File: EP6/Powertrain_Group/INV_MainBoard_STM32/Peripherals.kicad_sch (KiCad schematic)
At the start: 26 parts, among them U4 TCAN1042VDRQ1, U5 CAT24C256, U6 TCAN1042VDRQ1

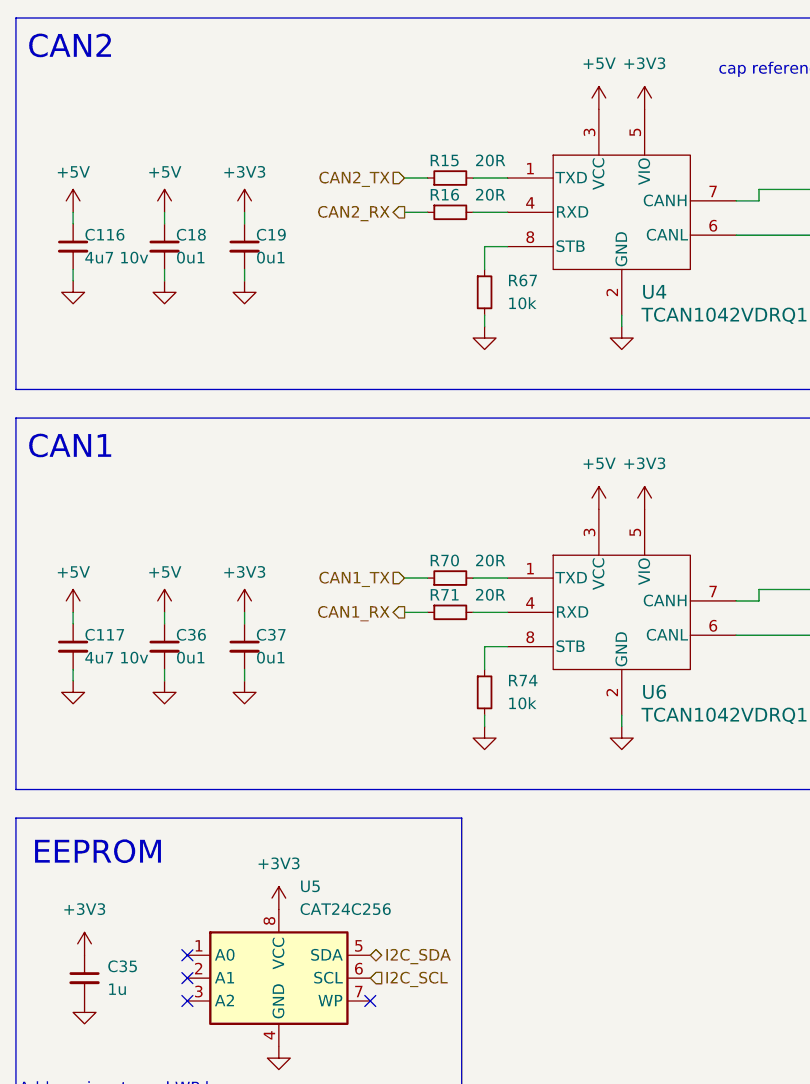
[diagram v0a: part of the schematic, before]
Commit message: update INV_MainBoard_STM32 to V2.1
update for JLCPCB, include change in 1.65 Vref and some name change for easier JLCPCBA BOM selection
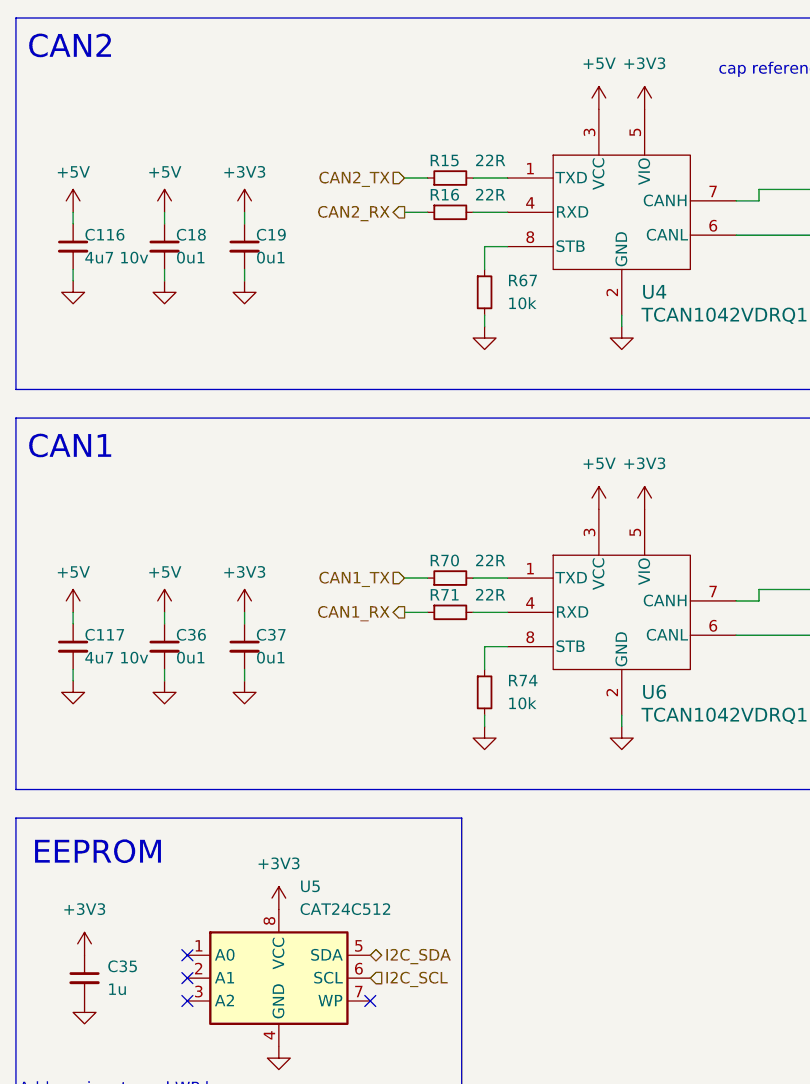
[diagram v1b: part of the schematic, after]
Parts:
- R15, R16, R70, R71: value 20R -> 22R
- U5: value CAT24C256 -> CAT24C512
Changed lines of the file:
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@@
 	(title_block
 		(title "INV_MainBoard_STM32")
-		(rev "2.0")
+		(date "2025-02-28")
+		(rev "2.1")
 		(company "NTURacing Team")
 		(comment 1 "郭哲明 Jack Kuo")
@@
 			)
 		)
-		(property "Value" "20R"
+		(property "Value" "22R"
 			(at 66.675 34.925 90)
 			(effects
@@
 			)
 		)
-		(property "Value" "CAT24C256"
+		(property "Value" "CAT24C512"
 			(at 45.4935 114.3 0)
 			(effects
@@
 			)
 		)
-		(property "Value" "20R"
+		(property "Value" "22R"
 			(at 66.675 31.115 90)
 			(effects
@@
 			)
 		)
-		(property "Value" "20R"
+		(property "Value" "22R"
 			(at 66.675 79.375 90)
 			(effects
@@
 			)
 		)
-		(property "Value" "20R"
+		(property "Value" "22R"
 			(at 66.675 75.565 90)
 			(effects

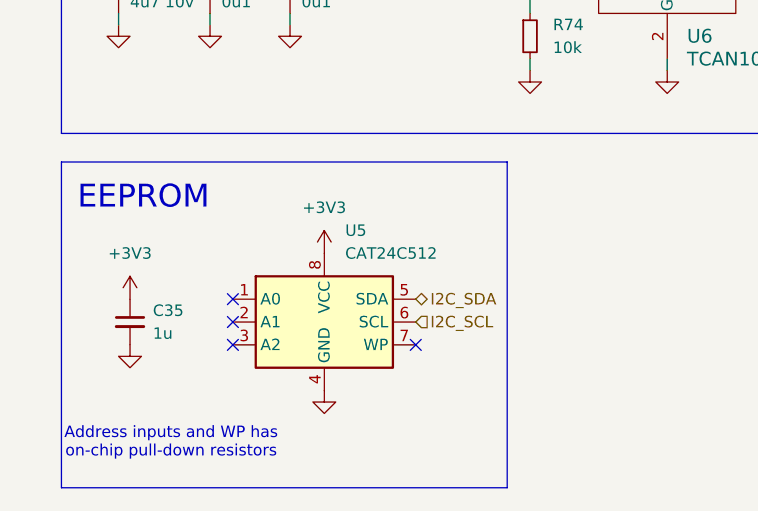
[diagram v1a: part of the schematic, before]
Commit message: update INV_MainBoard_STM32 to V3.0
PCB: INV_MainBoard_STM32 V3.0
V3.0 remove low volte trig
     add RC filt for OCP, OTP
     dedicated OTP, OCP pull down gate enable
     pending: fault hardware OTP/OCP latch
     pending: add QSPI DRAM
     use JST PH
     exterinal pull up for flt, ready
     fix CAN1, 2 label on board
     use 1k, 2k for encoder divider
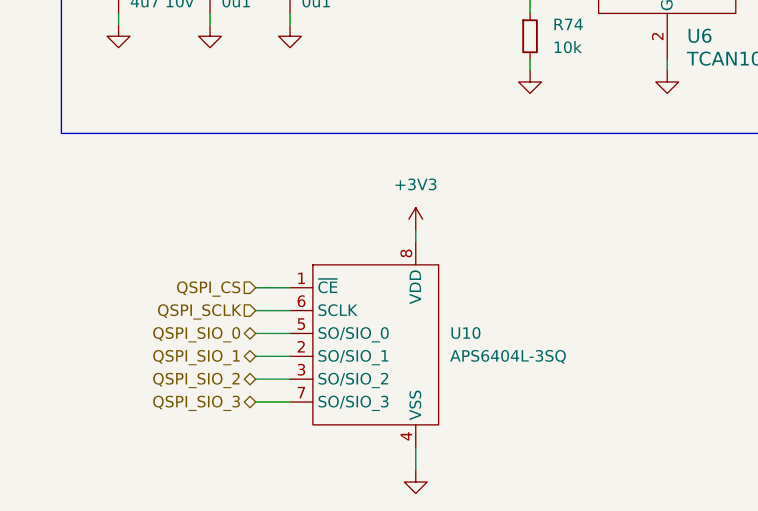
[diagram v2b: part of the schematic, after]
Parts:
- removed C35: 1u, Capacitor_SMD:C_0402_1005Metric, symbol Device:C_Small
- removed U5: CAT24C512, Package_SO:SOIC-8_3.9x4.9mm_P1.27mm, symbol Memory_EEPROM:CAT24C256
- added U10: APS6404L-3SQ, Package_SO:SOP-8_3.76x4.96mm_P1.27mm, symbol nturt_kicad_lib_EP6:APS6404L-3SQ
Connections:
- net +3V3: now also U10.8 (VDD)
- net GND: now also U10.4 (VSS)
- new net QSPI_CS: U10.1 (~{CE})
- new net QSPI_SCLK: U10.6 (SCLK)
- new net QSPI_SIO_0: U10.5 (SO/SIO_0)
- new net QSPI_SIO_1: U10.2 (SO/SIO_1)
- new net QSPI_SIO_2: U10.3 (SO/SIO_2)
- new net QSPI_SIO_3: U10.7 (SO/SIO_3)
- no-connect marks 4 -> 0
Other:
- note removed: "Address inputs and WP has on-chip pull-down resistors"
- note removed: "EEPROM"
